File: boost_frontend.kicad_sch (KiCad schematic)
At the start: 24 parts, among them U1 LT8342RV-TRMPBF

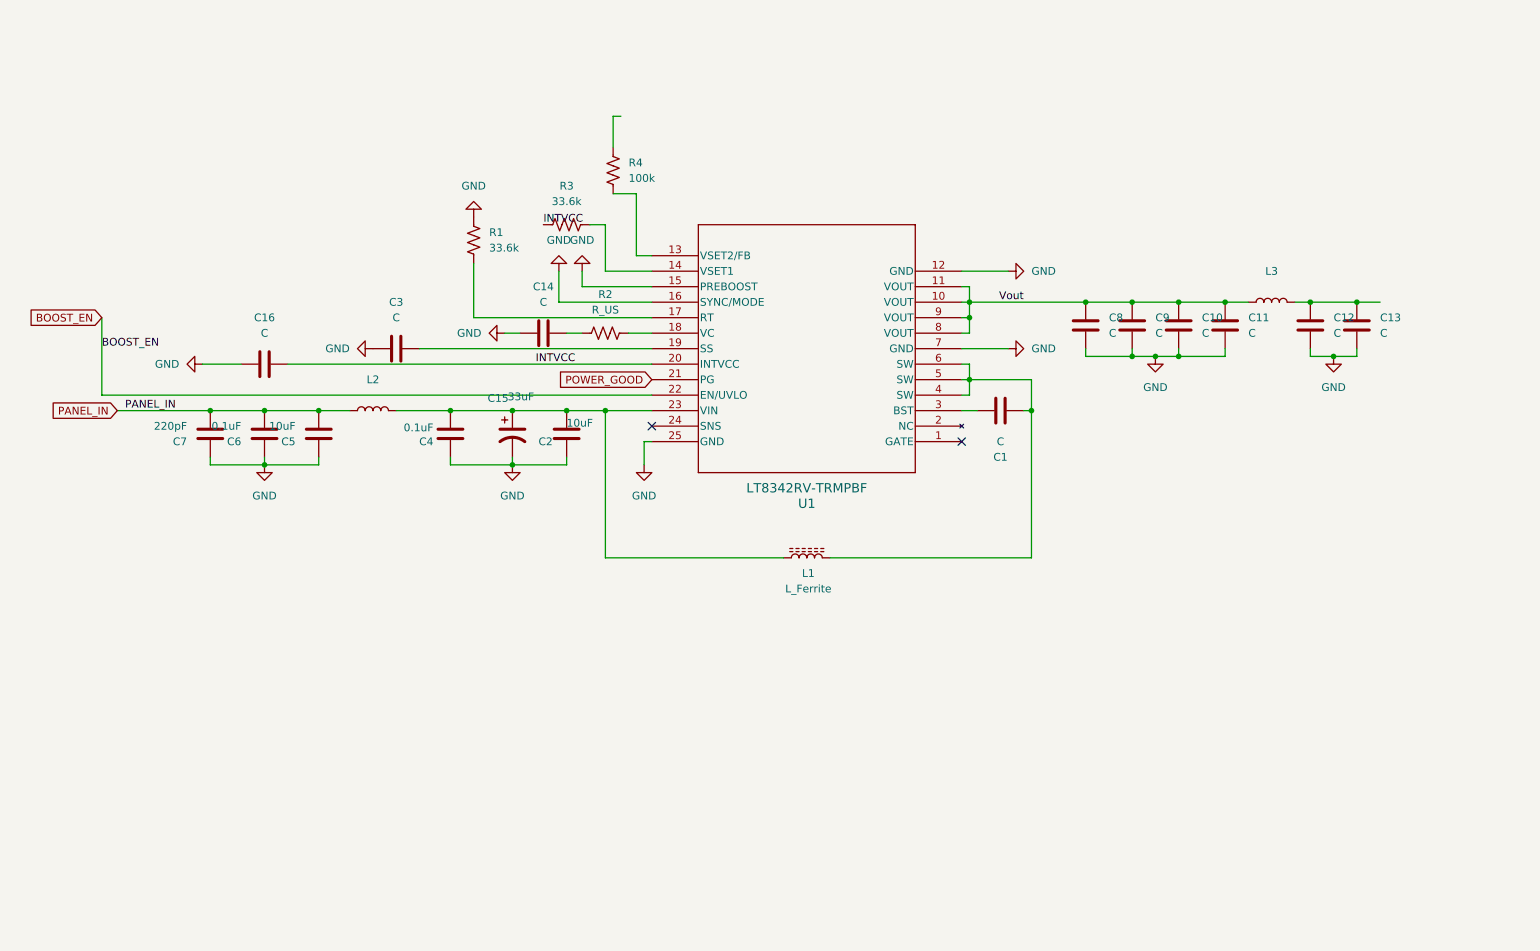
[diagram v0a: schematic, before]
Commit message: Adding passives to boost stage
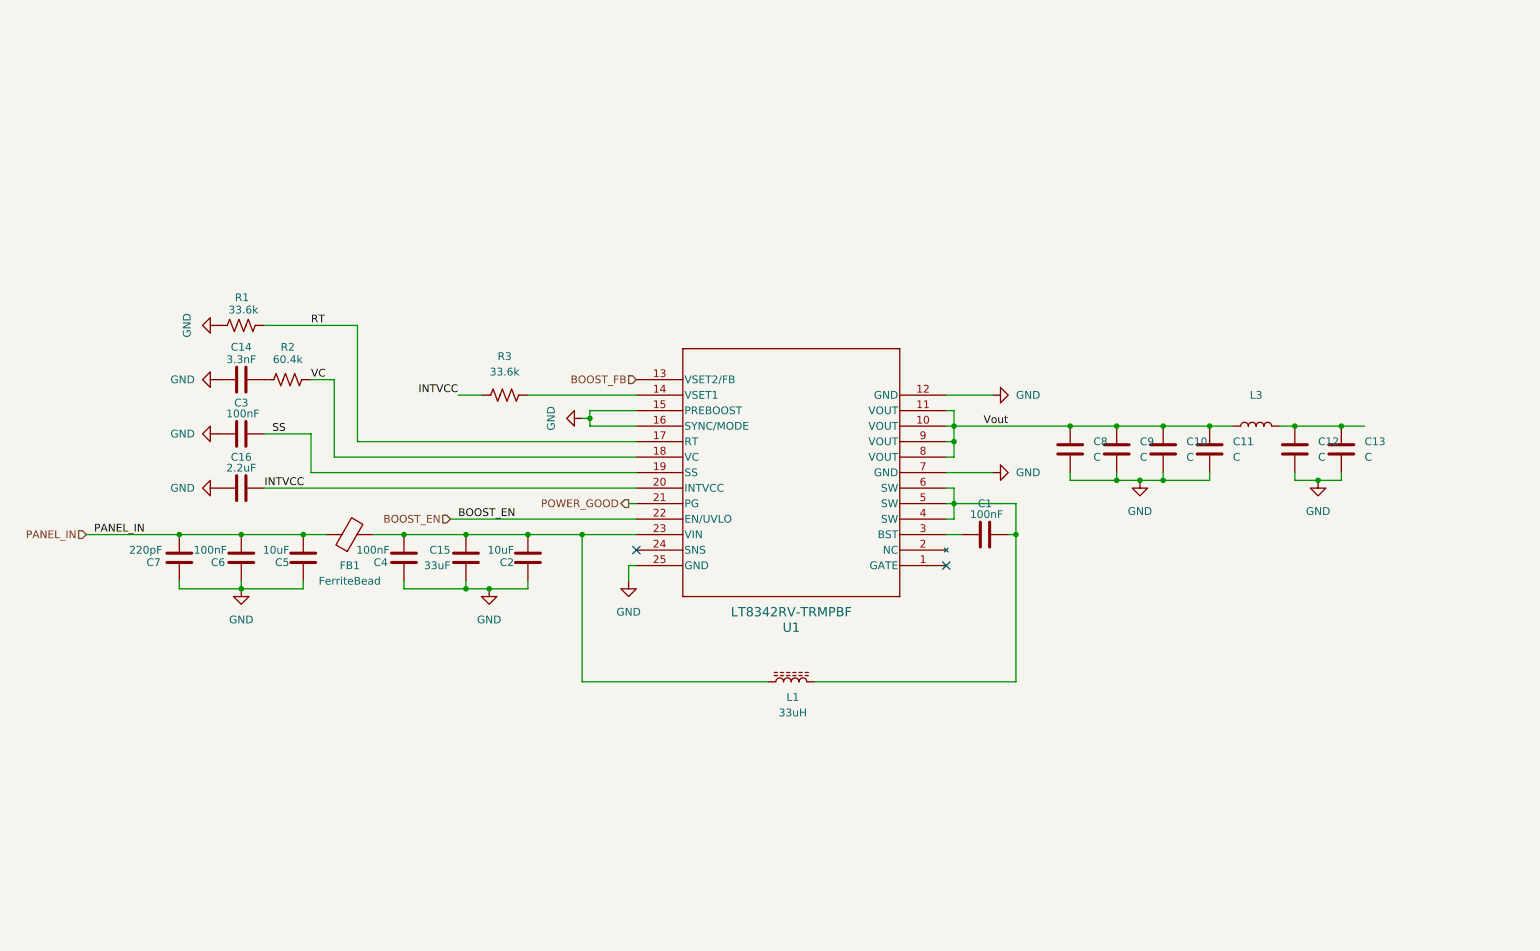
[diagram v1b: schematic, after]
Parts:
- removed C15: 33uF, symbol Device:C_Polarized_US
- removed L2: ~, symbol Device:L
- removed R4: 100k, symbol Device:R_US
- added C15: 33uF, Capacitor_SMD:C_1206_3216Metric, symbol Device:C
- added FB1: FerriteBead, Capacitor_SMD:C_2220_5750Metric, symbol Device:FerriteBead
- C1, C3: value C -> 100nF; footprint (none) -> Capacitor_SMD:C_1206_3216Metric; Mfr (none) -> Murata Electronics; Mfr P/N (none) -> GCM31C5C1H104FA16L; Supplier_1 (none) -> Digikey; Supplier_1 P/N (none) -> 490-GCM31C5C1H104FA16LTR-ND; Supplier_1 Price @ Qty (none) -> 1; Supplier_1 Unit Price (none) -> 0.98000
- C14: value C -> 3.3nF; footprint (none) -> Capacitor_SMD:C_0201_0603Metric; Mfr (none) -> Murata Electronics; Mfr P/N (none) -> GCM1885C1H332FA16D; Supplier_1 (none) -> Digikey; Supplier_1 P/N (none) -> 490-GCM1885C1H332FA16DTR-ND; Supplier_1 Price @ Qty (none) -> 1; Supplier_1 Unit Price (none) -> 0.17000
- C16: value C -> 2.2uF; footprint (none) -> Capacitor_SMD:C_0805_2012Metric; Mfr (none) -> KEMET; Mfr P/N (none) -> C0805C225J4RECTU; Supplier_1 (none) -> Digikey; Supplier_1 P/N (none) -> 399-C0805C225J4RECTUTR-ND; Supplier_1 Price @ Qty (none) -> 1; Supplier_1 Unit Price (none) -> 0.27000
- C2, C5: footprint (none) -> Capacitor_SMD:C_0805_2012Metric; Mfr (none) -> Murata Electronics; Mfr P/N (none) -> GRM21BR61H106KE43L; Supplier_1 (none) -> Digikey; Supplier_1 P/N (none) -> 490-18663-2-ND; Supplier_1 Price @ Qty (none) -> 1; Supplier_1 Unit Price (none) -> 0.28000
- C4, C6: value 0.1uF -> 100nF; footprint (none) -> Capacitor_SMD:C_1206_3216Metric; Mfr (none) -> Murata Electronics; Mfr P/N (none) -> GCM31C5C1H104FA16L; Supplier_1 (none) -> Digikey; Supplier_1 P/N (none) -> 490-GCM31C5C1H104FA16LTR-ND; Supplier_1 Price @ Qty (none) -> 1; Supplier_1 Unit Price (none) -> 0.98000
- C7: footprint (none) -> Capacitor_SMD:C_0603_1608Metric; Mfr (none) -> Murata Electronics; Mfr P/N (none) -> GCM1885C2A221FA16J; Supplier_1 (none) -> Digikey; Supplier_1 P/N (none) -> 490-GCM1885C2A221FA16JTR-ND; Supplier_1 Price @ Qty (none) -> 1; Supplier_1 Unit Price (none) -> 0.14000
- L1: value L_Ferrite -> 33uH; footprint (none) -> _Power_Board:IND_SER2918H-333KL; Mfr (none) -> Coilcraft; Mfr P/N (none) -> SER2918H-333KL; Supplier_1 (none) -> Digikey; Supplier_1 P/N (none) -> 2457-SER2918H-333KL-ND; Supplier_1 Price @ Qty (none) -> 1; Supplier_1 Unit Price (none) -> 6.98000
- R2: value R_US -> 60.4k
- U1: footprint 05-08-7040_ADI -> _Power_Board:05-08-7040_ADI; Mfr (none) -> Analog Devices Inc.; Mfr P/N (none) -> LT8342RV#TRPBF; Supplier_1 (none) -> Digikey; Supplier_1 P/N (none) -> 505-LT8342RV#TRPBFTR-ND; Supplier_1 Price @ Qty (none) -> 1; Supplier_1 Unit Price (none) -> 11.03000
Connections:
- net GND: now also C4.2, C6.2, C15.1; no longer C4.1, C6.1
- net INTVCC: now also R3.1; no longer R3.2
- net PANEL_IN: now also C6.1, FB1.1; no longer C6.2
- net at C2.2, L1.1, U1.23 (VIN): now also C4.1, C15.2, FB1.2; no longer C4.2
- net BOOST_FB: now reaches U1.13 (VSET2/FB)
- net RT: now reaches R1.1, U1.17 (RT)
- net VC: now reaches R2.2, U1.18 (VC)
- net at L1.2, U1.4 (SW), U1.5 (SW)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: now also C1.2; no longer C1.1
- net SS: now reaches C3.2, U1.19 (SS)
- net at U1.14 (VSET1): now also R3.2; no longer R3.1
- net at U1.3 (BST): now also C1.1; no longer C1.2
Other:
- moved on the sheet: C10, C11, C12, C13, C14, C16, C3, C5, C7, C8, C9, L1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

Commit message: Working on power board
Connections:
- net BOOST_OUT: now reaches C12.1, C13.1, L3.2
- net POWER_GOOD: no longer names the net of U1.21 (PG)
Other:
- moved on the sheet: C14, C16, C3, R1, R2, R3

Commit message: Working on 5v supply
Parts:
- removed C15: 33uF, Capacitor_SMD:C_1206_3216Metric, symbol Device:C
- removed L3: ~, symbol Device:L
- added C36: 33uF, Capacitor_SMD:CP_Elec_6.3x5.8, symbol Device:C_Polarized_US
- added FB2: 74279252, Inductor_SMD:L_1812_4532Metric, symbol Device:FerriteBead
- C1, C3, C4, C6: footprint Capacitor_SMD:C_1206_3216Metric -> Capacitor_SMD:C_0603_1608Metric; Mfr Murata Electronics -> KYOCERA AVX; Mfr P/N GCM31C5C1H104FA16L -> 06035C104K4T2A; Supplier_1 P/N 490-GCM31C5C1H104FA16LTR-ND -> 478-KAM15AR71H104KTTR-ND; Supplier_1 Unit Price 0.98000 -> 0.10000
- C10, C11: value C -> 10uF; footprint (none) -> Capacitor_SMD:C_0805_2012Metric; Mfr (none) -> Murata Electronics; Mfr P/N (none) -> GRM21BR61H106KE43L; Supplier_1 (none) -> Digikey; Supplier_1 P/N (none) -> 490-18663-2-ND; Supplier_1 Price @ Qty (none) -> 1; Supplier_1 Unit Price (none) -> 0.28000
- C12, C8, C9: value C -> 100nF; footprint (none) -> Capacitor_SMD:C_0603_1608Metric; Mfr (none) -> KYOCERA AVX; Mfr P/N (none) -> 06035C104K4T2A; Supplier_1 (none) -> Digikey; Supplier_1 P/N (none) -> 478-KAM15AR71H104KTTR-ND; Supplier_1 Price @ Qty (none) -> 1; Supplier_1 Unit Price (none) -> 0.10000
- C13: value C -> 220pF; footprint (none) -> Capacitor_SMD:C_0603_1608Metric; Mfr (none) -> Murata Electronics; Mfr P/N (none) -> GCM1885C2A221FA16J; Supplier_1 (none) -> Digikey; Supplier_1 P/N (none) -> 490-GCM1885C2A221FA16JTR-ND; Supplier_1 Price @ Qty (none) -> 1; Supplier_1 Unit Price (none) -> 0.14000
- C14: footprint Capacitor_SMD:C_0201_0603Metric -> Capacitor_SMD:C_0603_1608Metric
- C16: footprint Capacitor_SMD:C_0805_2012Metric -> Capacitor_SMD:C_0603_1608Metric; Mfr KEMET -> Murata Electronics; Mfr P/N C0805C225J4RECTU -> GRT188R61H225KE13D; Supplier_1 P/N 399-C0805C225J4RECTUTR-ND -> 490-12332-2-ND
- R1, R3: footprint (none) -> Resistor_SMD:R_0603_1608Metric; Mfr (none) -> KOA Speer Electronics, Inc.; Mfr P/N (none) -> RN73R1JTTD3362B25; Supplier_1 (none) -> Digikey; Supplier_1 P/N (none) -> 2019-RN73R1JTTD3362B25TR-ND; Supplier_1 Price @ Qty (none) -> 1; Supplier_1 Unit Price (none) -> 0.04314
- R2: footprint (none) -> Resistor_SMD:R_0603_1608Metric; Mfr (none) -> KOA Speer Electronics, Inc.; Mfr P/N (none) -> RN73H1JTTD6042B25; Supplier_1 (none) -> Digikey; Supplier_1 P/N (none) -> 2019-RN73H1JTTD6042B25TR-ND; Supplier_1 Price @ Qty (none) -> 1; Supplier_1 Unit Price (none) -> 0.10000
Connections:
- net BOOST_OUT: now also C13.2, FB2.2; no longer C13.1
- net GND: now also C10.1, C11.1, C13.1, C4.1, C6.1, R1.1, C36.2; no longer C10.2, C11.2, C13.2, C4.2, C6.2, R1.2
- net PANEL_IN: now also C6.2; no longer C6.1
- net RT: now also R1.2; no longer R1.1
- net Vout: now also C10.2, C11.2, FB2.1; no longer C10.1, C11.1
- net at C1.1: now also L1.2, U1.4 (SW), U1.5 (SW), U1.6 (SW); no longer U1.3 (BST)
- net at C2.2, FB1.2, L1.1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: now also C4.2, C36.1; no longer C4.1
- net PGOOD: now reaches U1.21 (PG)
- net BOOST_EN renamed EN
- net BOOST_FB renamed FB
- new net: C1.2, U1.3 (BST)
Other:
- note added: "Compensation network"
- note added: "Control scheme"
- company: (none) -> Solar Airplane
- title: (none) -> Boost front-end
- moved on the sheet: R3

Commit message: Adding control stuff
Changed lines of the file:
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@@
 		(dnp no)
 		(property "Reference" "C8"
-			(at 199.39 91.44 0)
+			(at 199.644 91.186 0)
 			(effects
 				(font
@@
 		)
 		(property "Value" "100nF"
-			(at 197.612 89.408 0)
+			(at 197.866 89.154 0)
 			(effects
 				(font
@@
 		(dnp no)
 		(property "Reference" "C2"
-			(at 105.664 108.712 0)
+			(at 110.236 106.426 0)
 			(effects
 				(font
 					(size 1.27 1.27)
 				)
-				(justify left)
+				(justify right)
 			)
 		)
 		(property "Value" "10uF"
-			(at 105.664 106.68 0)
+			(at 110.236 108.458 0)
 			(effects
 				(font
 					(size 1.27 1.27)
 				)
-				(justify left)
+				(justify right)
 			)
 		)
@@
 		(on_board yes)
 		(dnp no)
-		(fields_autoplaced yes)
 		(property "Reference" "C36"
-			(at 101.6 106.0449 0)
+			(at 100.076 106.426 0)
 			(effects
 				(font
@@
 		)
 		(property "Value" "33uF"
-			(at 101.6 108.5849 0)
+			(at 100.076 108.458 0)
 			(effects
 				(font
@@
 		(dnp no)
 		(property "Reference" "C10"
-			(at 218.694 90.932 0)
+			(at 218.948 91.186 0)
 			(effects
 				(font
@@
 		)
 		(property "Value" "10uF"
-			(at 218.694 88.9 0)
+			(at 218.948 89.154 0)
 			(effects
 				(font
@@
 		(dnp no)
 		(property "Reference" "C11"
-			(at 227.584 90.932 0)
+			(at 227.838 91.186 0)
 			(effects
 				(font
@@
 		)
 		(property "Value" "10uF"
-			(at 227.584 88.9 0)
+			(at 227.838 89.154 0)
 			(effects
 				(font
@@
 		(dnp no)
 		(property "Reference" "C4"
-			(at 84.074 108.712 0)
+			(at 90.932 106.426 0)
 			(effects
 				(font
@@
 		)
 		(property "Value" "100nF"
-			(at 82.804 106.68 0)
+			(at 92.71 108.458 0)
 			(effects
 				(font

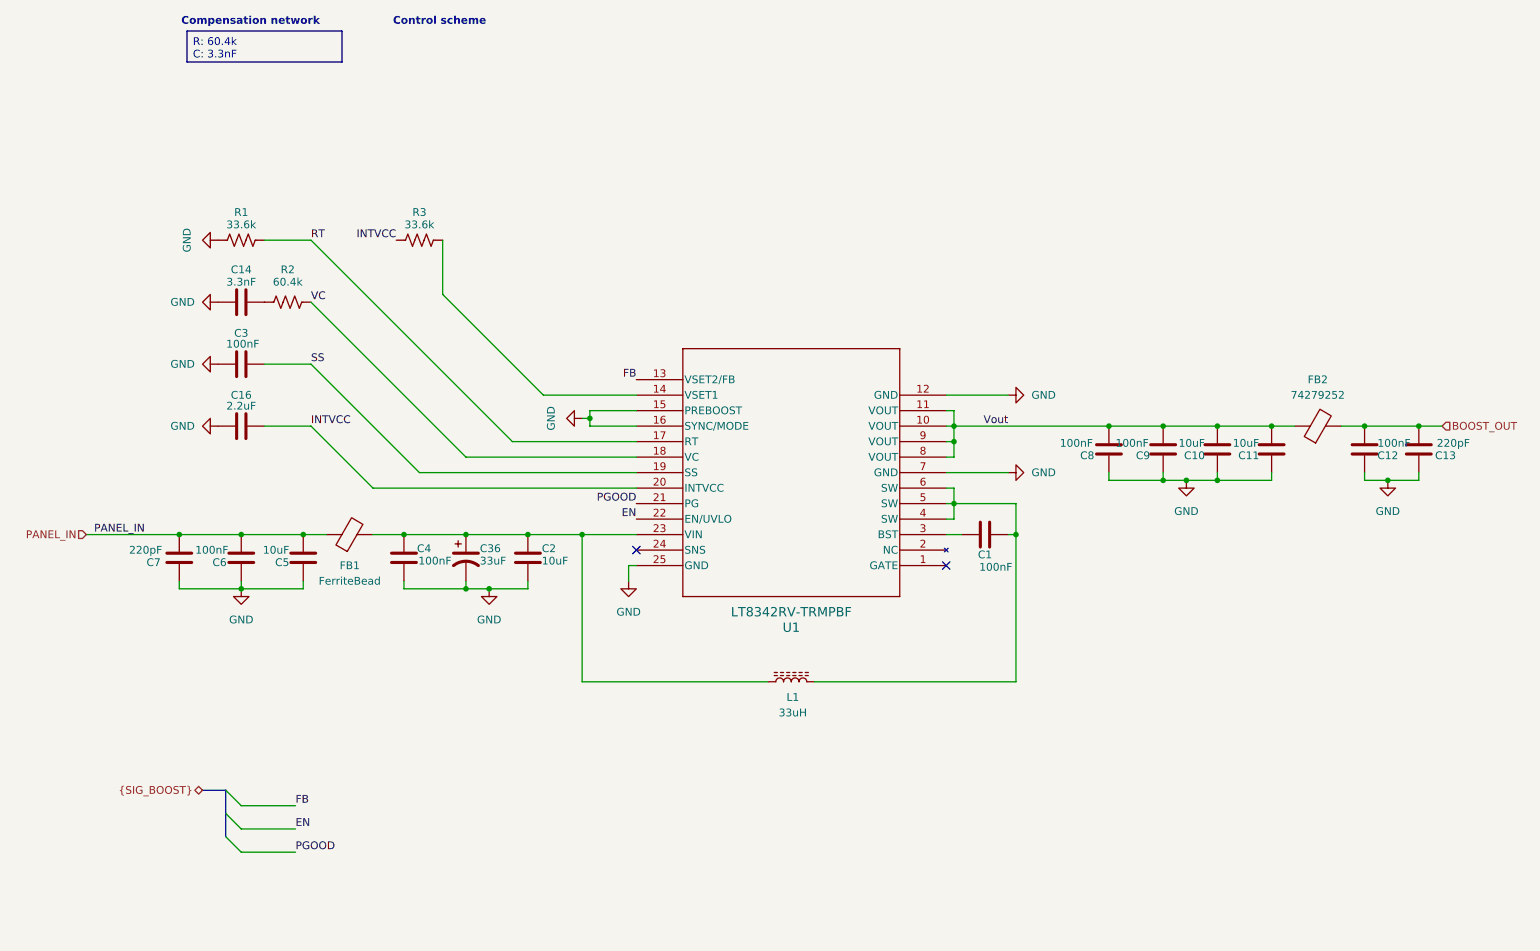
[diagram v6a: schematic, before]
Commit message: Adding in connections to schematic
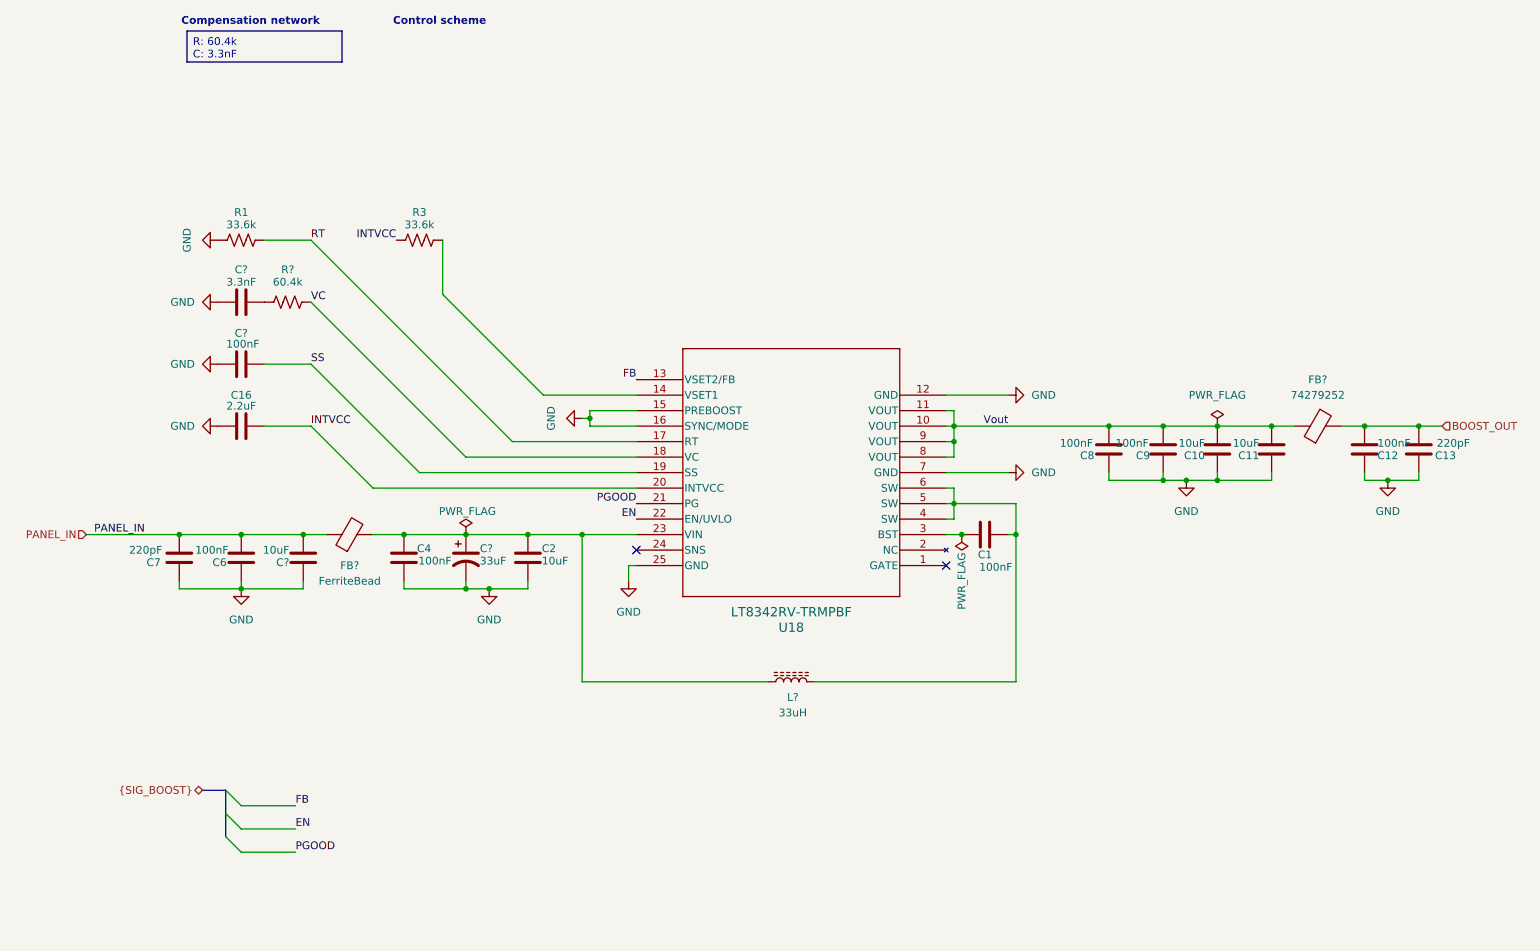
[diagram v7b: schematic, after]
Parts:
- renumbered C14 to C?, C5 to C?, C36 to C?, C3 to C?, FB1 to FB?, FB2 to FB?, L1 to L?, R2 to R?, U1 to U18

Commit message: Working on layout now
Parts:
- gave numbers to parts that had none: 8
- renumbered C7 to C1, C1 to C10, C8 to C11, C9 to C12, C10 to C13, C11 to C14, C12 to C15, C13 to C16, C16 to C4, C6 to C5, C4 to C7, C2 to C9, U18 to U1
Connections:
- net RT: no longer names the net of R1.2, U1.17 (RT)
- net SS: no longer names the net of C3.2, U1.19 (SS)
- net VC: no longer names the net of R2.2, U1.18 (VC)
